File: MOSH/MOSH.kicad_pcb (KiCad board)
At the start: 2 copper layers, 68.6 x 53.3 mm, 8 parts, among them J1 Power, J2 Digital/PWM, J3 Analog, J4 Digital/PWM

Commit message: add all footprints and start rooting
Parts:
- added C1: 100n, Capacitor_THT:C_Disc_D4.7mm_W2.5mm_P5.00mm, F.Cu at (125.0, 94.0)
- added C2: 1u, Capacitor_THT:C_Rect_L7.0mm_W4.5mm_P5.00mm, F.Cu at (129.0, 89.0)
- added C3: 100n, Capacitor_THT:C_Disc_D4.7mm_W2.5mm_P5.00mm, F.Cu at (103.0, 84.0)
- added C4: 100n, Capacitor_THT:C_Disc_D4.7mm_W2.5mm_P5.00mm, F.Cu at (153.3, 64.4)
- added C5: 100n, Capacitor_THT:C_Disc_D4.7mm_W2.5mm_P5.00mm, F.Cu at (130.0, 70.0)
- added C6: 100n, Capacitor_THT:C_Disc_D4.7mm_W2.5mm_P5.00mm, F.Cu at (134.0, 76.0)
- added J5: Conn_01x08_Socket, Connector_PinSocket_2.54mm:PinSocket_1x08_P2.54mm_Vertical, F.Cu at (158.4, 56.8)
- added J6: Conn_01x03_Pin, Connector_PinHeader_2.54mm:PinHeader_1x03_P2.54mm_Vertical, F.Cu at (107.0, 71.0)
- added Q1: IRF540N, Package_TO_SOT_THT:TO-220-3_Vertical, F.Cu at (119.0, 84.0)
- added R1: 10k, Resistor_THT:R_Axial_DIN0207_L6.3mm_D2.5mm_P10.16mm_Horizontal, F.Cu at (125.0, 64.0)
- added R2: 100k, Resistor_THT:R_Axial_DIN0207_L6.3mm_D2.5mm_P10.16mm_Horizontal, F.Cu at (113.0, 84.0)
- added R4: 100k, Resistor_THT:R_Axial_DIN0207_L6.3mm_D2.5mm_P10.16mm_Horizontal, F.Cu at (161.0, 79.7)
- added R5: 1k, Resistor_THT:R_Axial_DIN0207_L6.3mm_D2.5mm_P10.16mm_Horizontal, F.Cu at (127.9, 79.7)
- added R6: 100k, Resistor_THT:R_Axial_DIN0207_L6.3mm_D2.5mm_P10.16mm_Horizontal, F.Cu at (141.0, 93.0)
- added R7: 10k, Resistor_THT:R_Axial_DIN0207_L6.3mm_D2.5mm_P10.16mm_Horizontal, F.Cu at (118.0, 76.0)
- added R8: 1k, Resistor_THT:R_Axial_DIN0207_L6.3mm_D2.5mm_P10.16mm_Horizontal, F.Cu at (143.2, 61.9)
- added U1: LTC1050, Package_DIP:DIP-8_W7.62mm, F.Cu at (142.0, 79.0)
- added U2: MCP41100, Package_DIP:DIP-8_W7.62mm, F.Cu at (138.1, 54.3)
- added U3: ~, Package_TO_SOT_THT:TO-5-10, F.Cu at (113.0, 64.0)
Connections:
- J1 pad 4: +3V3 -> +3.3V
- J2 pad 5: /13 -> SCK
- J2 pad 7: /*11 -> MOSI
- J2 pad 8: /*10 -> CS
- J3 pad 1: /A0 -> ADC
- J3 pad 2: /A1 -> VTEMP
- J4 pad 2: /*6 -> PWM
- J4 pad 4: /4 -> RST
- J4 pad 5: /*3 -> TX
- J4 pad 6: /2 -> RX
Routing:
- net RST: track 0.00 -> 20.6 mm
- net GND: track 0.00 -> 17.2 mm
- net R3: track 0.00 -> 16.1 mm
- net TX: track 0.00 -> 12.1 mm
- net RX: track 0.00 -> 7.62 mm
- net CS: track 0.00 -> 5.71 mm
- net MOSI: track 0.00 -> 5.50 mm

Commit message: router avec Allan!
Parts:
- moved R6 59.3 mm to (191.4, 61.9)
- moved R7 57.6 mm to (67.0, 49.2)
- moved J6 53.2 mm to (158.4, 84.8), turned to 90 degrees
- moved Q1 50.6 mm to (82.2, 49.2)
- moved R8 48.5 mm to (191.4, 56.8)
- moved R4 42.6 mm to (120.3, 92.4), turned to 0 degrees
- moved U3 31.9 mm to (141.9, 77.4), turned to 180 degrees
- moved C4 30.6 mm to (140.6, 92.3), turned to 90 degrees
- moved C5 27.4 mm to (145.8, 92.4)
- moved R5 20.5 mm to (107.6, 82.3), turned to 90 degrees
- moved R2 20.1 mm to (117.8, 64.4), turned to -90 degrees
- moved C1 17.1 mm to (112.7, 82.1)
- moved C6 16.5 mm to (135.6, 92.4), turned to 90 degrees
- moved U1 12.3 mm to (130.5, 74.6), turned to -90 degrees
- moved R1 12.3 mm to (112.7, 64.4), turned to -90 degrees
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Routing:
- net ADC: track 0.00 -> 70.4 mm
- net Net-(C2-Pad2): track 0.00 -> 41.7 mm
- net +5V: track 0.00 -> 27.0 mm
- net Net-(U1-+): track 0.00 -> 18.0 mm
- net GND: track 17.2 -> 0.00 mm
- net SCK: track 0.00 -> 15.6 mm
- net R3: track 16.1 -> 21.8 mm
- net VCC: track 0.00 -> 5.11 mm
- net +3.3V: track 0.00 -> 5.08 mm

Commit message: je pensais avoir commit la dernière fois
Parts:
- moved J6 23.4 mm to (140.6, 69.5), turned to -90 degrees
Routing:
- net ISENS2: track 0.00 -> 13.1 mm
- net +5V: track 27.0 -> 39.5 mm
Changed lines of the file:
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@@
   )
   (footprint "Connector_PinHeader_2.54mm:PinHeader_1x03_P2.54mm_Vertical" placed (layer "F.Cu")
-    (at 158.42 84.76 90)
+    (at 140.64 69.52 -90)
     (descr "Through hole straight pin header, 1x03, 2.54mm pitch, single row")
     (tags "Through hole pin header THT 1x03 2.54mm single row")
@@
     (fp_line (start 1.27 6.35) (end -1.27 6.35)
       (stroke (width 0.1) (type solid)) (layer "F.Fab"))
-    (pad "1" thru_hole rect (at 0 0 90) (size 1.7 1.7) (drill 1) (layers "*.Cu" "*.Mask")
+    (pad "1" thru_hole rect (at 0 0 270) (size 1.7 1.7) (drill 1) (layers "*.Cu" "*.Mask")
       (net 32 "ISENS1") (pinfunction "Pin_1") (pintype "passive"))
-    (pad "2" thru_hole oval (at 0 2.54 90) (size 1.7 1.7) (drill 1) (layers "*.Cu" "*.Mask")
+    (pad "2" thru_hole oval (at 0 2.54 270) (size 1.7 1.7) (drill 1) (layers "*.Cu" "*.Mask")
       (net 33 "Net-(J6-Pin_2)") (pinfunction "Pin_2") (pintype "passive"))
-    (pad "3" thru_hole oval (at 0 5.08 90) (size 1.7 1.7) (drill 1) (layers "*.Cu" "*.Mask")
+    (pad "3" thru_hole oval (at 0 5.08 270) (size 1.7 1.7) (drill 1) (layers "*.Cu" "*.Mask")
       (net 34 "ISENS2") (pinfunction "Pin_3") (pintype "passive"))
     (model "${KICAD6_3DMODEL_DIR}/Connector_PinHeader_2.54mm.3dshapes/PinHeader_1x03_P2.54mm_Vertical.wrl"
@@
   )
   (segment (start 136.05127 84.76) (end 129.34863 84.76) (width 1.2) (layer "B.Cu") (net 3))
+  (segment (start 138.1 78.174271) (end 139.90466 79.978931) (width 1.2) (layer "B.Cu") (net 3))
   (segment (start 138.1 94.84) (end 140.64 92.3) (width 1.2) (layer "B.Cu") (net 3))
   (segment (start 127.94 83.35137) (end 127.94 82.22) (width 1.2) (layer "B.Cu") (net 3))
   (segment (start 129.34863 84.76) (end 127.94 83.35137) (width 1.2) (layer "B.Cu") (net 3))
   (segment (start 138.1 94.84) (end 138.1 86.80873) (width 1.2) (layer "B.Cu") (net 3))
+  (segment (start 139.90466 80.90661) (end 136.05127 84.76) (width 1.2) (layer "B.Cu") (net 3))
+  (segment (start 139.90466 80.15417) (end 139.90466 80.90661) (width 1.2) (layer "B.Cu") (net 3))
+  (segment (start 138.1 74.6) (end 138.1 78.174271) (width 1.2) (layer "B.Cu") (net 3))
+  (segment (start 139.90466 79.978931) (end 139.90466 80.15417) (width 1.2) (layer "B.Cu") (net 3))
   (segment (start 138.1 86.80873) (end 136.05127 84.76) (width 1.2) (layer "B.Cu") (net 3))
   (segment (start 138.1 97.46) (end 138.1 94.84) (width 1.2) (layer "B.Cu") (net 3))
@@
   (segment (start 138.1 54.28) (end 138.1 51.083138) (width 0.8) (layer "B.Cu") (net 16))
   (segment (start 136.576 49.559138) (end 136.576 49.2) (width 0.8) (layer "B.Cu") (net 16))
-  (segment (start 107.62 95.005584) (end 112.139416 99.525) (width 0.8) (layer "B.Cu") (net 17))
+  (segment (start 112.139416 99.525) (end 148.735 99.525) (width 0.8) (layer "B.Cu") (net 17))
   (segment (start 107.62 92.38) (end 107.62 95.005584) (width 0.8) (layer "B.Cu") (net 17))
   (segment (start 107.62 72.14) (end 105.62 74.14) (width 0.8) (layer "B.Cu") (net 17))
+  (segment (start 148.735 99.525) (end 150.8 97.46) (width 0.8) (layer "B.Cu") (net 17))
   (segment (start 105.62 90.38) (end 107.62 92.38) (width 0.8) (layer "B.Cu") (net 17))
-  (segment (start 112.139416 99.525) (end 148.735 99.525) (width 0.8) (layer "B.Cu") (net 17))
-  (segment (start 148.735 99.525) (end 150.8 97.46) (width 0.8) (layer "B.Cu") (net 17))
+  (segment (start 107.62 95.005584) (end 112.139416 99.525) (width 0.8) (layer "B.Cu") (net 17))
   (segment (start 105.62 74.14) (end 105.62 90.38) (width 0.8) (layer "B.Cu") (net 17))
   (segment (start 156 62.02) (end 153.34 59.36) (width 0.8) (layer "B.Cu") (net 21))
@@
   (segment (start 145.72 97.46) (end 145.72 92.46) (width 1.2) (layer "B.Cu") (net 27))
   (segment (start 112.7 97.54) (end 112.78 97.46) (width 1.2) (layer "B.Cu") (net 27))
+  (segment (start 133.02 77.14) (end 134.973418 79.093418) (width 0.8) (layer "B.Cu") (net 34))
+  (segment (start 134.973418 79.093418) (end 136.64 79.093418) (width 0.8) (layer "B.Cu") (net 34))
+  (segment (start 133.02 72.06) (end 133.02 77.14) (width 0.8) (layer "B.Cu") (net 34))
+  (segment (start 135.56 69.52) (end 133.02 72.06) (width 0.8) (layer "B.Cu") (net 34))
   (segment (start 127.94 74.6) (end 127.94 75.73137) (width 0.8) (layer "B.Cu") (net 38))
   (segment (start 120.32 81.931572) (end 120.32 87.3) (width 0.8) (layer "B.Cu") (net 38))

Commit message: je route
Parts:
- moved R7 95.4 mm to (153.3, 89.8), turned to 90 degrees
- moved Q1 70.3 mm to (150.8, 64.4), turned to -90 degrees
- moved R8 45.8 mm to (145.7, 54.3), turned to -90 degrees
- moved R6 44.9 mm to (158.4, 92.4), turned to 90 degrees
- moved U2 7.62 mm to (130.5, 54.3)
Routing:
- net +5V: track 39.5 -> 90.1 mm
- net VTEMP: track 0.00 -> 39.9 mm
- net Net-(J6-Pin_2): track 0.00 -> 32.9 mm
- net SCK: track 15.6 -> 38.4 mm
- net R3: track 21.8 -> 36.6 mm
- net VHEAT: track 0.00 -> 13.8 mm
- net VCC: track 5.11 -> 15.2 mm
- net MOSI: track 5.50 -> 12.1 mm
- net ISENS1: track 0.00 -> 6.44 mm
- net PWM: track 0.00 -> 6.13 mm
- net Net-(Q1-G): track 0.00 -> 5.08 mm
- net CS: track 5.71 -> 8.93 mm
- net ISENS2: track 13.1 -> 11.2 mm
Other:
- board size 68.6 x 53.3 mm -> 68.6 x 55.9 mm

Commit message: routage fini oui j'ai fait des vias, du coup il manque plus que le plan de masse
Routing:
- net +3.3V: track 5.08 -> 70.3 mm
- net VHEAT: track 13.8 -> 30.1 mm, vias 0 -> 2
- net ADC: track 70.4 -> 74.6 mm, vias 0 -> 1
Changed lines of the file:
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@@
   (segment (start 138.1 97.46) (end 138.1 94.84) (width 1.2) (layer "B.Cu") (net 3))
   (segment (start 138.1 82.982598) (end 140.1 80.982598) (width 1.2) (layer "B.Cu") (net 3))
+  (segment (start 165.75 95.305) (end 165.75 98.391981) (width 1.2) (layer "B.Cu") (net 5))
+  (segment (start 158.42 69.52) (end 159.622081 69.52) (width 1.2) (layer "B.Cu") (net 5))
   (segment (start 135.56 92.38) (end 135.56 97.46) (width 1.2) (layer "B.Cu") (net 5))
+  (segment (start 159.622081 69.52) (end 163.84 73.737919) (width 1.2) (layer "B.Cu") (net 5))
+  (segment (start 163.84 93.395) (end 165.75 95.305) (width 1.2) (layer "B.Cu") (net 5))
+  (segment (start 163.84 73.737919) (end 163.84 93.395) (width 1.2) (layer "B.Cu") (net 5))
+  (segment (start 164.141981 100) (end 136.897919 100) (width 1.2) (layer "B.Cu") (net 5))
+  (segment (start 136.897919 100) (end 135.56 98.662081) (width 1.2) (layer "B.Cu") (net 5))
+  (segment (start 165.75 98.391981) (end 164.141981 100) (width 1.2) (layer "B.Cu") (net 5))
+  (segment (start 135.56 98.662081) (end 135.56 97.46) (width 1.2) (layer "B.Cu") (net 5))
   (segment (start 117.491573 54.28) (end 120.32 54.28) (width 0.8) (layer "B.Cu") (net 6))
   (segment (start 127.94 55.41137) (end 127.07137 56.28) (width 0.8) (layer "B.Cu") (net 6))
@@
   (segment (start 136.576 50.446742) (end 132.742742 54.28) (width 0.8) (layer "B.Cu") (net 16))
   (segment (start 132.742742 54.28) (end 130.48 54.28) (width 0.8) (layer "B.Cu") (net 16))
-  (segment (start 112.124416 99.51) (end 148.75 99.51) (width 0.8) (layer "B.Cu") (net 17))
+  (segment (start 147.785 102.065) (end 148.26 102.065) (width 0.8) (layer "F.Cu") (net 17))
+  (segment (start 148.26 102.065) (end 148.26 97.46) (width 0.8) (layer "F.Cu") (net 17))
+  (via (at 147.785 102.065) (size 0.6) (drill 0.4) (layers "F.Cu" "B.Cu") (net 17))
+  (segment (start 107.62 93.938427) (end 115.746573 102.065) (width 0.8) (layer "B.Cu") (net 17))
   (segment (start 107.62 72.14) (end 105.62 74.14) (width 0.8) (layer "B.Cu") (net 17))
-  (segment (start 107.62 95.005584) (end 112.124416 99.51) (width 0.8) (layer "B.Cu") (net 17))
+  (segment (start 107.62 92.38) (end 107.62 93.938427) (width 0.8) (layer "B.Cu") (net 17))
+  (segment (start 115.746573 102.065) (end 147.785 102.065) (width 0.8) (layer "B.Cu") (net 17))
   (segment (start 105.62 90.38) (end 107.62 92.38) (width 0.8) (layer "B.Cu") (net 17))
-  (segment (start 107.62 92.38) (end 107.62 95.005584) (width 0.8) (layer "B.Cu") (net 17))
+  (segment (start 150.8 97.46) (end 148.26 97.46) (width 0.8) (layer "B.Cu") (net 17))
   (segment (start 105.62 74.14) (end 105.62 90.38) (width 0.8) (layer "B.Cu") (net 17))
-  (segment (start 148.75 99.51) (end 150.8 97.46) (width 0.8) (layer "B.Cu") (net 17))
   (segment (start 158.42 82.22) (end 146.765245 82.22) (width 0.8) (layer "B.Cu") (net 19))
   (segment (start 158.42 82.22) (end 160.42 84.22) (width 0.8) (layer "B.Cu") (net 19))
@@
   (segment (start 145.72 94.92) (end 145.72 92.46) (width 1.2) (layer "B.Cu") (net 27))
   (segment (start 150.22873 89.84) (end 145.72 94.34873) (width 1.2) (layer "B.Cu") (net 27))
-  (segment (start 112.7 97.54) (end 112.78 97.46) (width 1.2) (layer "B.Cu") (net 27))
   (segment (start 145.72 94.34873) (end 145.72 94.92) (width 1.2) (layer "B.Cu") (net 27))
   (segment (start 153.34 89.84) (end 150.22873 89.84) (width 1.2) (layer "B.Cu") (net 27))
-  (segment (start 141.36466 70.24466) (end 141.36466 75.660752) (width 0.8) (layer "B.Cu") (net 32))
-  (segment (start 140.64 69.52) (end 141.36466 70.24466) (width 0.8) (layer "B.Cu") (net 32))
+  (segment (start 140.64 69.52) (end 141.70466 70.58466) (width 0.8) (layer "B.Cu") (net 32))
+  (segment (start 141.70466 70.58466) (end 141.70466 75.345585) (width 0.8) (layer "B.Cu") (net 32))
   (segment (start 138.1 69.52) (end 138.1 66.691572) (width 0.8) (layer "B.Cu") (net 33))
   (segment (start 117.24 59.9) (end 112.7 64.44) (width 0.8) (layer "B.Cu") (net 33))
@@
   (segment (start 135.791472 79.093418) (end 136.64 79.093418) (width 0.8) (layer "B.Cu") (net 34))
   (segment (start 150.8 64.44) (end 145.72 64.44) (width 0.8) (layer "B.Cu") (net 35))
-  (segment (start 153.34 69.52) (end 153.34 79.68) (width 0.8) (layer "B.Cu") (net 36))
-  (segment (start 150.8 66.98) (end 153.34 69.52) (width 0.8) (layer "B.Cu") (net 36))
+  (segment (start 143.30466 72.06) (end 140.20516 72.06) (width 0.8) (layer "F.Cu") (net 36))
+  (via (at 143.30466 72.06) (size 0.6) (drill 0.4) (layers "F.Cu" "B.Cu") (net 36))
+  (via (at 140.20516 72.06) (size 0.6) (drill 0.4) (layers "F.Cu" "B.Cu") (net 36))
+  (segment (start 149.095 66.98) (end 144.015 72.06) (width 0.8) (layer "B.Cu") (net 36))
+  (segment (start 153.34 67.815) (end 153.34 79.68) (width 0.8) (layer "B.Cu") (net 36))
+  (segment (start 139.90466 72.26) (end 140.10466 72.06) (width 0.8) (layer "B.Cu") (net 36))
+  (segment (start 144.015 72.06) (end 143.30466 72.06) (width 0.8) (layer "B.Cu") (net 36))
+  (segment (start 139.90466 74.6) (end 139.90466 72.26) (width 0.8) (layer "B.Cu") (net 36))
+  (segment (start 150.8 66.98) (end 149.095 66.98) (width 0.8) (layer "B.Cu") (net 36))
+  (segment (start 152.505 66.98) (end 153.34 67.815) (width 0.8) (layer "B.Cu") (net 36))
+  (segment (start 150.8 66.98) (end 152.505 66.98) (width 0.8) (layer "B.Cu") (net 36))
   (segment (start 127.94 74.6) (end 127.94 75.73137) (width 0.8) (layer "B.Cu") (net 38))
   (segment (start 120.32 81.931572) (end 120.32 87.3) (width 0.8) (layer "B.Cu") (net 38))

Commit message: commencer le plan de masse, mon routage il est tout cassé du coup
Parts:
- removed MH4: MountingHole_3.2mm, Arduino_MountingHole:MountingHole_3.2mm
- moved R6 11.4 mm to (148.3, 87.3)
- moved C4 5.00 mm to (140.6, 87.3), turned to -90 degrees
- moved R4 4.02 mm to (116.5, 93.7)
- moved C2 4.02 mm to (116.5, 88.6)
- moved C1 2.86 mm to (110.2, 83.5)
- moved R1 2.54 mm to (110.2, 64.4)
- moved R2 2.54 mm to (115.2, 64.4)
- moved R5 2.54 mm to (105.1, 82.3)
- moved U1 2.54 mm to (127.9, 74.6)
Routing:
- net ADC: track 74.6 -> 0.00 mm, vias 1 -> 0
- net Net-(J6-Pin_2): track 32.9 -> 0.00 mm
- net +5V: track 90.1 -> 62.4 mm
- net Net-(C2-Pad2): track 41.7 -> 14.2 mm
- net +3.3V: track 70.3 -> 78.1 mm
- net VTEMP: track 39.9 -> 35.4 mm
- net R3: track 36.6 -> 32.4 mm
- net SCK: track 38.4 -> 39.6 mm
- net Net-(U1-+): track 18.0 -> 19.0 mm
- added copper zone on B.Cu, net GND
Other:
- board size 68.6 x 55.9 mm -> 68.6 x 61 mm

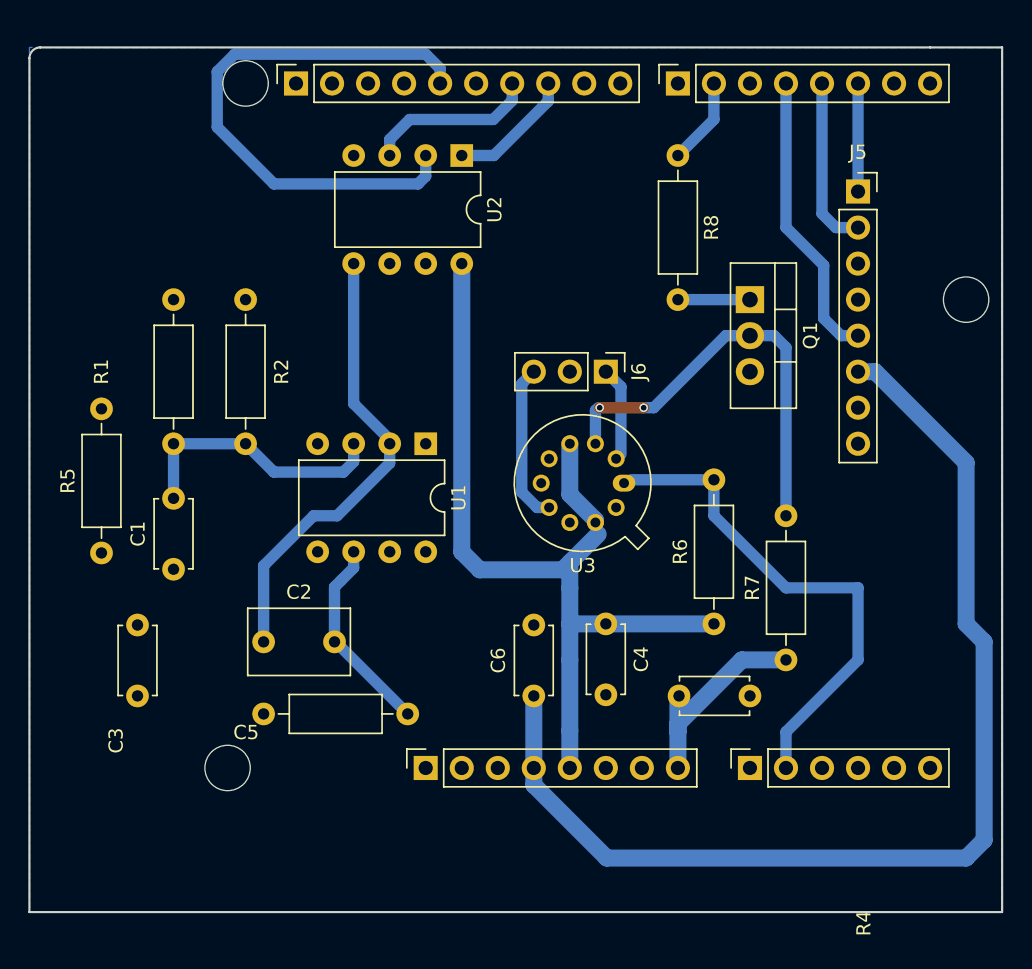
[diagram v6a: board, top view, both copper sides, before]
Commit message: presque fini routage il manque plus que quelques détails ; penser à checker les règles electrique
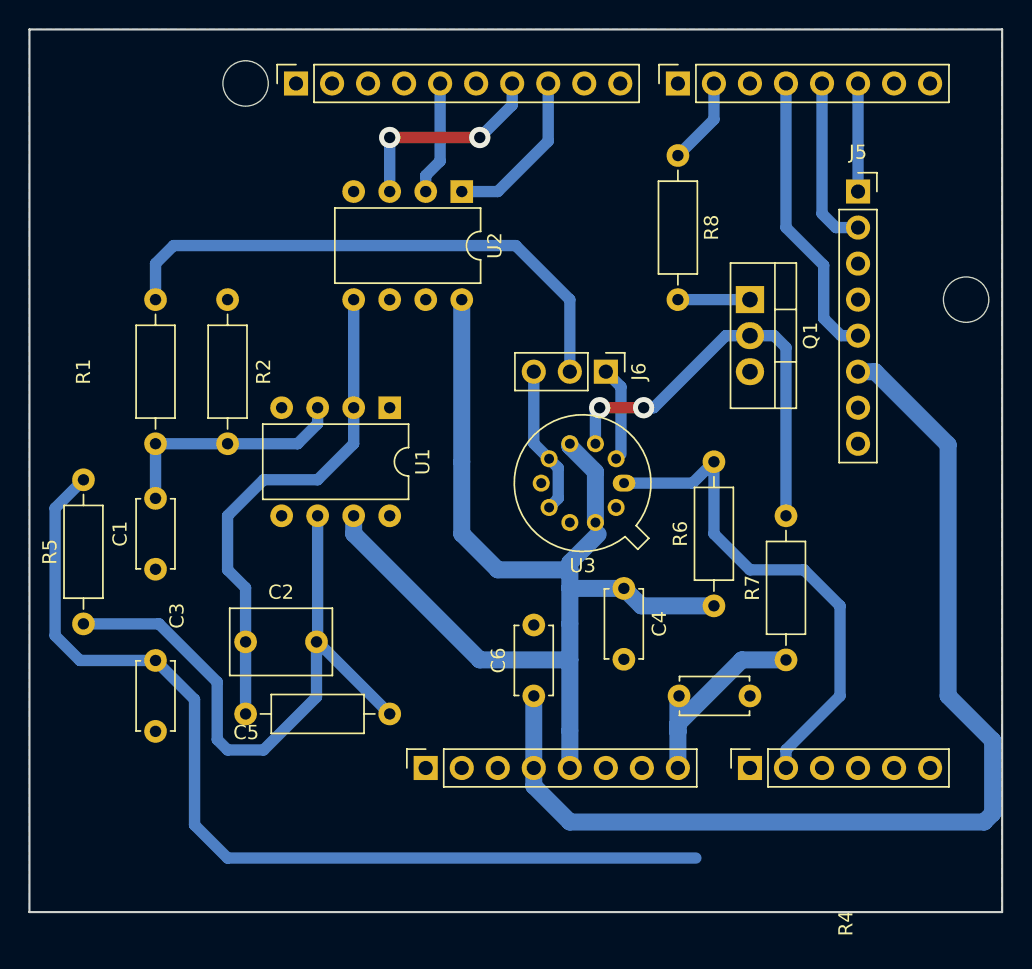
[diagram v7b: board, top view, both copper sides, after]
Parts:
- removed MH2: MountingHole_3.2mm, Arduino_MountingHole:MountingHole_3.2mm
- moved R5 5.16 mm to (103.8, 87.3)
- moved U1 3.59 mm to (125.4, 72.1)
- moved C4 2.80 mm to (141.9, 84.8)
- moved C3 2.80 mm to (108.9, 89.9), turned to -90 degrees
- moved U2 2.54 mm to (130.5, 56.8)
- moved C2 1.27 mm to (115.2, 88.6)
- moved R4 1.27 mm to (115.2, 93.7)
- moved C1 1.27 mm to (108.9, 83.5)
- moved R1 1.27 mm to (108.9, 64.4)
- moved R2 1.27 mm to (114.0, 64.4)
- moved R6 1.27 mm to (148.3, 86.0)
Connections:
- U3 pad 5: unconnected-(U3-NC-Pad5) -> ISENS2
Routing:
- net ADC: track 0.00 -> 68.7 mm
- net Net-(J6-Pin_2): track 0.00 -> 38.9 mm
- net SCK: track 39.6 -> 8.04 mm
- net Net-(C2-Pad2): track 14.2 -> 44.1 mm
- net +5V: track 62.4 -> 79.7 mm
- net R3: track 32.4 -> 35.7 mm
- net MOSI: track 12.1 -> 14.9 mm, vias 0 -> 2
- net CS: track 8.93 -> 11.6 mm
- net +3.3V: track 78.1 -> 75.8 mm
- net Net-(U1-+): track 19.0 -> 17.0 mm
- net ISENS2: track 11.2 -> 10.6 mm
- net VTEMP: track 35.4 -> 36.0 mm
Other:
- board size 68.6 x 61 mm -> 68.6 x 62.2 mm
